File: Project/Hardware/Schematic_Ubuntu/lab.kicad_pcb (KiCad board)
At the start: 2 copper layers, 56 parts, among them J1 USB_B_Micro, J2 6P Male, J3 Conn_01x03_Male, Q1 2N3904, SW1 SW_SPDT, U1 NCP1117-3.3_SOT223, U10 MomentSwitch, U11 MomentSwitch, U2 STM32F411RETx, U3 lis3dh_board, U4 Pulse_sensor, U5 MAX4460ESA+, U6 Nokia5110, U7 piezo, U8 MomentSwitch, U9 MomentSwitch, Y1 8MHz

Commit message: Pcb rev 4
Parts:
- U5: footprint TO_SOT_Packages_SMD:SOT-23-8_Handsoldering -> Housings_SOIC:SO-8_5.3x6.2mm_Pitch1.27mm
- moved SW1 97.4 mm to (175.5, 83.3), turned to 180 degrees
- moved BT1 87.8 mm to (180.8, 89.2)
- moved C2 75.2 mm to (181.1, 76.7), turned to 90 degrees
- moved J1 74.4 mm to (174.2, 90.7)
- moved C1 72.3 mm to (177.0, 77.5), turned to 90 degrees
- moved C16 65.2 mm to (99.3, 62.7), turned to 0 degrees
- moved C4 52.1 mm to (171.4, 77.5)
- moved R2 51.7 mm to (118.6, 72.9), turned to 270 degrees
- moved U1 51.0 mm to (166.1, 88.9), turned to 90 degrees
- moved U3 49.9 mm to (106.7, 58.2)
- moved C19 44.9 mm to (131.8, 86.4)
- moved U6 42.5 mm to (139.4, 70.3)
- moved R12 40.9 mm to (147.6, 81.6), turned to 270 degrees
- moved C5 40.7 mm to (166.1, 80.8), turned to 180 degrees
- moved R17 37.5 mm to (168.0, 70.9), turned to 90 degrees
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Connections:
- U2 pad 10: /LCD_DC -> Net-(U2-Pad10)
- U2 pad 22: /TIM3_CH1 -> Net-(U2-Pad22)
- U2 pad 24: Net-(U2-Pad24) -> /LCD_RST
- U2 pad 25: Net-(U2-Pad25) -> /LCD_SCE
- U2 pad 26: /TIM_START -> /LCD_DC
- U2 pad 27: /TIM_INC -> Net-(U2-Pad27)
- U2 pad 28: /TIM_RES -> Net-(U2-Pad28)
- U2 pad 37: Net-(U2-Pad37) -> /TIM3_CH1
- U2 pad 38: Net-(U2-Pad38) -> /TIM_START
- U2 pad 39: Net-(U2-Pad39) -> /TIM_INC
- U2 pad 40: Net-(U2-Pad40) -> /TIM_RES
- U2 pad 8: /LCD_SCE -> Net-(U2-Pad8)
- U2 pad 9: /LCD_RST -> Net-(U2-Pad9)
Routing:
- net +3V3: track 304.2 -> 443.7 mm, vias 0 -> 7
- net /TIM_START: track 0.00 -> 51.4 mm, vias 0 -> 1
- net /TEMPOUT: track 0.00 -> 45.2 mm, vias 0 -> 2
- net /PULSESIG: track 0.00 -> 41.5 mm
- net /TIM_INC: track 0.00 -> 39.1 mm, vias 0 -> 1
- net /NRST: track 57.6 -> 95.8 mm, vias 2 -> 1
- net /SPI1_MOSI: track 49.5 -> 14.0 mm, vias 2 -> 0
- net /TIM_RES: track 0.00 -> 33.9 mm, vias 0 -> 1
- net /PIEZOPWM: track 24.7 -> 53.6 mm
- net /I2C1_SCL: track 19.6 -> 47.7 mm
- net /LCD_RST: track 43.9 -> 16.3 mm
- net /SPI1_SCK: track 44.0 -> 18.9 mm, vias 2 -> 0
- net /USART1_RX: track 0.00 -> 23.6 mm
- net /LCD_SCE: track 43.2 -> 20.0 mm
- net /USART1_TX: track 0.00 -> 22.8 mm
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- added copper zone on B.Cu, net GND
- added copper zone on F.Cu, net GND
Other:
- board outline added: 87.8 x 48.1 mm
- net class GND_SMALL added: clearance 0.15, trace_width 0.3, via_dia 0.8, via_drill 0.3
- net class Power: trace_width 0.2 -> 0.4
- board text added: "PASC REV S"

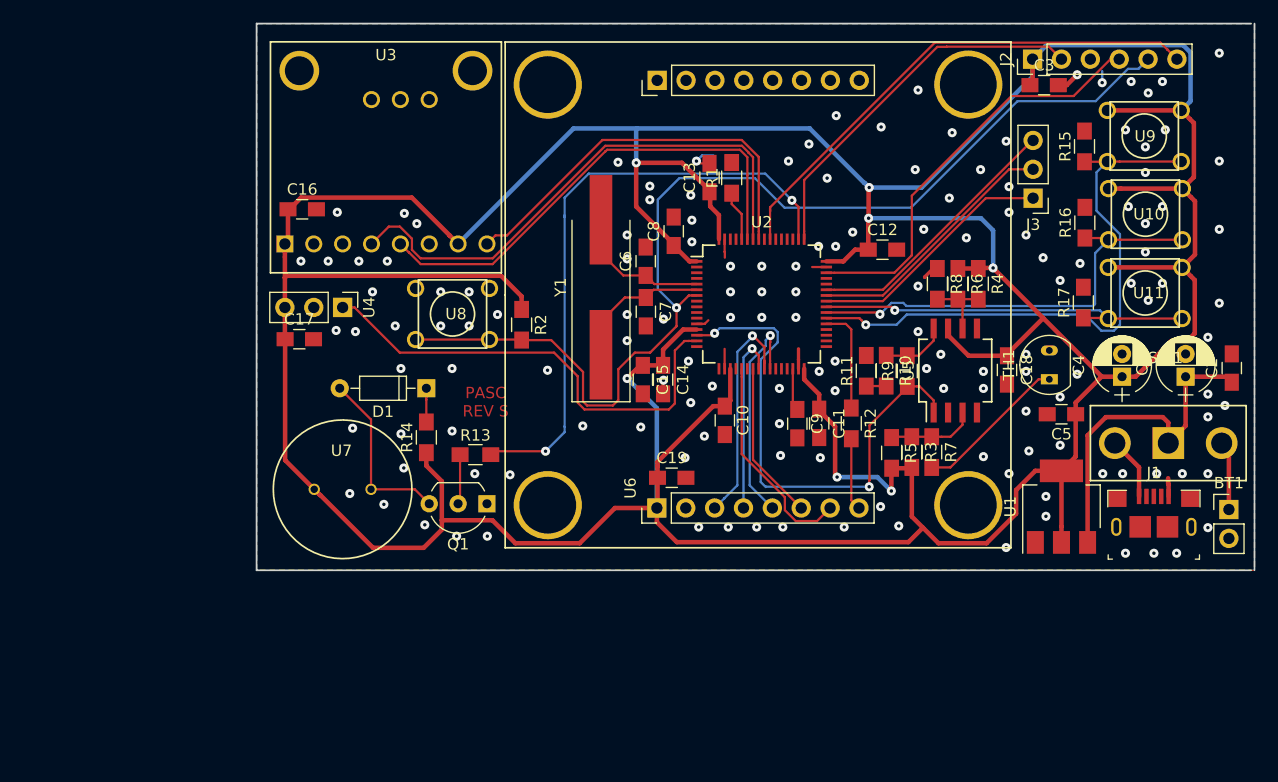
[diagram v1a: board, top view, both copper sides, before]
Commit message: Extra resistor till temp gain, två cubemx project med olika pinsmaps, Gerber filer till pcb_revS
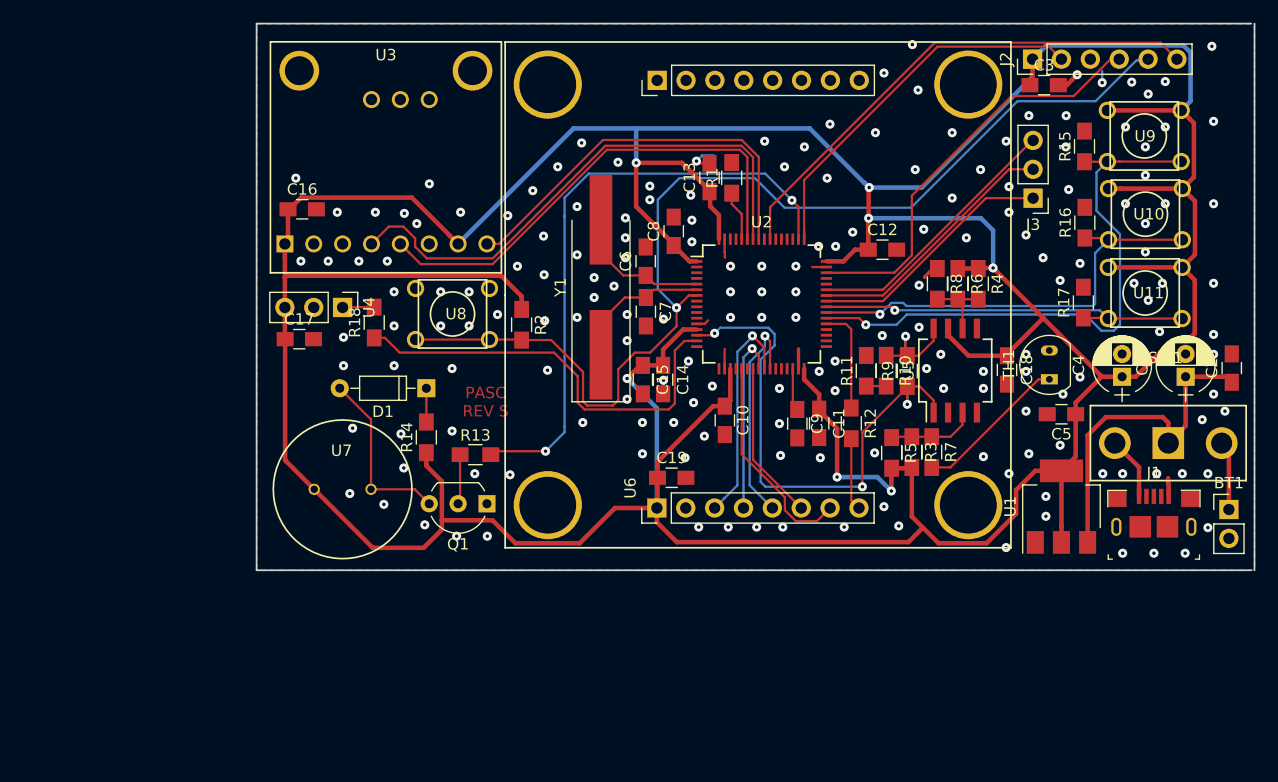
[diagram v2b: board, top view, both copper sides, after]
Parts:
- added R18: 1k, Resistors_SMD:R_0805_HandSoldering, F.Cu at (105.7, 72.7)
- added R19: 100k, Resistors_SMD:R_0805_HandSoldering, B.Cu at (152.6, 77.0)
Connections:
- U4 pad 1: /PULSESIG -> Net-(R18-Pad2)
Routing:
- net /PULSESIG: track 41.5 -> 37.6 mm
- net /Temp Sensor/INAMPFB: track 5.93 -> 9.40 mm, vias 0 -> 1
- net Net-(R18-Pad2): track 0.00 -> 2.79 mm
- net /TEMPOUT: track 45.2 -> 47.5 mm, vias 2 -> 3
- net GND: vias 148 -> 180
